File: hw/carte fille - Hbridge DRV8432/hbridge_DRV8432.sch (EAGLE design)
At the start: 37 parts, among them IC1 DRV8402

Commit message: Start routing the board
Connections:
- net GND: no longer C15.1, C16.1, C19.1, C20.1
- net GVDD: no longer R1.2, R11.2, R2.2, R3.2
- net N$1: no longer R3.1
- net N$16: now also IC1.RESET_AB; no longer IC1.RESET_CD, R11.1
- net N$17: now also IC1.PWM_B; no longer IC1.PWM_A
- net N$18: now also IC1.PWM_C; no longer IC1.PWM_B
- net N$19: now also IC1.RESET_CD; no longer IC1.PWM_C
- net N$6: no longer R2.1
- net N$8: now also IC1.PWM_A; no longer IC1.RESET_AB, R1.1
- net PVDD: no longer C15.2, C16.2, C19.2, C20.2
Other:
- moved on the sheet: SIGNAL

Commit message: rework board routing
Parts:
- removed C10, C11, C12, C13, C15, C16, C19, C20: 100nF - 0805, resistor:C-EUC0805
- removed C14: 100n, etienne:C_NP_805
- removed C18: 47uF, etienne:CPOL-EUE3.5-8
- removed C22: 330µF, etienne:CPOL-EUE3.5-8
- removed C5: 10nF - 0805, resistor:C-EUC0805
- removed SIGNAL: (no value), con-lsta:FE09-1
- added C17: 47u, rcl:CPOL-EUB/3528-21W
- added C21: 1u, rcl:C-EUC0805
- added C31, C32, C33, C34: 100n, rcl:C-EUC0805
- added C35, C36, C37, C38: 100n, rcl:C-EUC0603
- added H1, H2, H3, H4: MOUNT-HOLE3.2, holes:MOUNT-HOLE3.2
- added JP1: (no value), pinhead-2:PINHD-1X08_2.54
- added X4: M1-2, con-wago-500:W237-102
- added X5: M3-4, con-wago-500:W237-102
- added X6: +12V, con-wago-500:W237-102
- added X7: +24V, con-wago-500:W237-102
- C1: value 10nF - 0805 -> 10n; device resistor:C-EUC0805 -> rcl:C-EUC0805
- C2, C6, C8: value 1uF - 0805 -> 1u; device resistor:C-EUC0805 -> rcl:C-EUC0805
- C3: value 1000uF -> 1000u; device etienne:CPOL-EUE3.5-8 -> rcl:CPOL-EUE3.5-10
- C4: value 1000uF -> 100n; device etienne:CPOL-EUE3.5-8 -> rcl:C-EUC0603K
- C7: value 1uF -0805 -> 1u; device resistor:C-EUC0805 -> rcl:C-EUC0805
- C9: value 1uF - 0805 -> 330u; device resistor:C-EUC0805 -> rcl:CPOL-EUB/3528-21W
- R10: value 3R3 - 0603 -> 3.3; device resistor:R-EU_R0603 -> rcl:R-EU_R1206
- R12: value 3R3 - 0603 -> (none); device resistor:R-EU_R0603 -> rcl:R-EU_R0603
- R9: value 27K - 0603 -> 1; device resistor:R-EU_R0603 -> rcl:R-EU_R0603
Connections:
- removed net N$14: C5.1, R12.2
- removed net N$15: C13.1, IC1.BST_A
- removed net N$22: R5.1, X1-3.1
- removed net OUT_A: C13.2, IC1.OUT_A, X2-1.1
- removed net OUT_B: C12.2, IC1.OUT_B, X2-2.1
- removed net OUT_C: C11.2, IC1.OUT_C, X3-1.1
- removed net OUT_D: C10.2, IC1.OUT_D, X3-2.1
- new net GND1: X6-1.KL, X7-1.KL
- new net M1A: C33.1, IC1.OUT_A, X2-1.1, X4-1.KL
- new net M1B: C32.1, IC1.OUT_B, X2-2.1, X4-2.KL
- new net M1C: C31.2, IC1.OUT_C, X3-1.1, X5-1.KL
- new net M1D: C34.2, IC1.OUT_D, X3-2.1, X5-2.KL
- new net N$25: C33.2, IC1.BST_A
- new net N$26: C32.2, IC1.BST_B
- new net N$27: C31.1, IC1.BST_C
- new net N$28: C34.1, IC1.BST_D
- net GND: now also C1.1, C17.-, C2.1, C21.1, C35.1, C36.1, C37.1, C38.1, C6.1, C7.1, C8.1, C9.-, R9.1, X1-4.1; no longer C1.2, C14.1, C18.-, C2.2, C22.-, C4.-, C5.2, C6.2, C7.2, C8.2, C9.2, IC1.AGND, R4.2, R7.2, R8.2, R9.2, SIGNAL.1, X1-1.1
- net GVDD: now also C17.+, C2.2, C21.2, C6.2, C7.2, C8.2, C9.+; no longer C18.+, C2.1, C22.+, C6.1, C7.1, C8.1, C9.1
- net N$1: now also JP1.8; no longer SIGNAL.9
- net N$10: now also IC1.OC_ADJ, R12.2; no longer C12.1, IC1.BST_B
- net N$11: now also C4.1; no longer C14.2
- net N$12: now also X1-2.1; no longer C10.1, IC1.BST_D
- net N$13: now also C1.2, R10.1; no longer C1.1, R10.2
- net N$16: now also JP1.5; no longer SIGNAL.6
- net N$17: now also JP1.4; no longer SIGNAL.5
- net N$18: now also JP1.3; no longer SIGNAL.4
- net N$19: now also JP1.2; no longer SIGNAL.3
- net N$2: now also X1-1.1, X6-2.KL; no longer X1-2.1
- net N$20: now also JP1.1; no longer SIGNAL.2
- net N$6: now also JP1.7; no longer SIGNAL.8
- net N$7: now also R5.1, X1-3.1, X7-2.KL; no longer C11.1, IC1.BST_C
- net N$8: now also JP1.6; no longer SIGNAL.7
- net N$9: now also C4.2, IC1.AGND, R12.1, R4.2, R7.2, R8.2, R9.2; no longer IC1.OC_ADJ, R9.1
- net PVDD: now also C35.2, C36.2, C37.2, C38.2, R10.2; no longer C4.+, R10.1, R12.1
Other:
- moved on the sheet: C1, C2, C3, C6, C7, C8, R10, R12, R6, R9, X2-1, X2-2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

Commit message: wip
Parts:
- removed R5, R6: 0R, resistor:R-EU_R0603
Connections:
- removed net GND1: X6-1.KL, X7-1.KL
- removed net N$2: R6.1, X1-1.1, X6-2.KL
- removed net N$7: R5.1, X1-3.1, X7-2.KL
- net GND: now also X6-1.KL, X7-1.KL
- net GVDD: now also X1-1.1, X6-2.KL; no longer R6.2
- net PVDD: now also X1-3.1, X7-2.KL; no longer R5.2
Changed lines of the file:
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@@
 <part name="R7" library="resistor" deviceset="R-EU_" device="R0603" value="0R"/>
 <part name="R8" library="resistor" deviceset="R-EU_" device="R0603" value="0R"/>
-<part name="R6" library="resistor" deviceset="R-EU_" device="R0603" value="0R"/>
 <part name="GND8" library="supply1" deviceset="GND" device=""/>
 <part name="X1" library="con-phoenix-254" deviceset="MPT4" device=""/>
-<part name="R5" library="resistor" deviceset="R-EU_" device="R0603" value="0R"/>
 <part name="X2" library="con-phoenix-254" deviceset="MPT2" device=""/>
 <part name="X3" library="con-phoenix-254" deviceset="MPT2" device=""/>
@@
 <part name="X6" library="con-wago-500" deviceset="W237-102" device="" value="+12V"/>
 <part name="X7" library="con-wago-500" deviceset="W237-102" device="" value="+24V"/>
+<part name="GND2" library="supply1" deviceset="GND" device=""/>
 </parts>
 <sheets>
@@
 <instance part="R7" gate="G$1" x="-30.48" y="-12.7" rot="R180"/>
 <instance part="R8" gate="G$1" x="-30.48" y="-15.24" rot="R180"/>
-<instance part="R6" gate="G$1" x="-119.38" y="78.74"/>
 <instance part="GND8" gate="1" x="-124.46" y="73.66"/>
 <instance part="X1" gate="-1" x="-132.08" y="78.74" rot="R180"/>
@@
 <instance part="X1" gate="-3" x="-132.08" y="88.9" rot="R180"/>
 <instance part="X1" gate="-4" x="-132.08" y="93.98" rot="R180"/>
-<instance part="R5" gate="G$1" x="-121.92" y="88.9"/>
 <instance part="X2" gate="-1" x="58.42" y="7.62"/>
 <instance part="X2" gate="-2" x="58.42" y="2.54"/>
@@
 <instance part="X7" gate="-1" x="-119.38" y="45.72" rot="R180"/>
 <instance part="X7" gate="-2" x="-119.38" y="50.8" rot="R180"/>
+<instance part="GND2" gate="1" x="-134.62" y="27.94"/>
 </instances>
 <busses>
@@
 </segment>
 <segment>
-<pinref part="R5" gate="G$1" pin="2"/>
-<wire x1="-116.84" y1="88.9" x2="-109.22" y2="88.9" width="0.1524" layer="91"/>
 <label x="-114.3" y="88.9" size="1.778" layer="95"/>
+<pinref part="X7" gate="-2" pin="KL"/>
+<wire x1="-124.46" y1="50.8" x2="-127" y2="50.8" width="0.1524" layer="91"/>
+<wire x1="-127" y1="50.8" x2="-127" y2="88.9" width="0.1524" layer="91"/>
+<pinref part="X1" gate="-3" pin="1"/>
+<wire x1="-129.54" y1="88.9" x2="-127" y2="88.9" width="0.1524" layer="91"/>
+<wire x1="-127" y1="88.9" x2="-109.22" y2="88.9" width="0.1524" layer="91"/>
 </segment>
 <segment>
@@
 </segment>
 <segment>
+<pinref part="X1" gate="-4" pin="1"/>
+<wire x1="-124.46" y1="93.98" x2="-129.54" y2="93.98" width="0.1524" layer="91"/>
 <pinref part="GND8" gate="1" pin="GND"/>
-<pinref part="X1" gate="-4" pin="1"/>
 <wire x1="-124.46" y1="76.2" x2="-124.46" y2="93.98" width="0.1524" layer="91"/>
-<wire x1="-124.46" y1="93.98" x2="-129.54" y2="93.98" width="0.1524" layer="91"/>
+</segment>
+<segment>
+<wire x1="-124.46" y1="45.72" x2="-134.62" y2="45.72" width="0.1524" layer="91"/>
+<wire x1="-134.62" y1="45.72" x2="-134.62" y2="33.02" width="0.1524" layer="91"/>
+<wire x1="-124.46" y1="33.02" x2="-134.62" y2="33.02" width="0.1524" layer="91"/>
+<pinref part="X7" gate="-1" pin="KL"/>
+<pinref part="X6" gate="-1" pin="KL"/>
+<pinref part="GND2" gate="1" pin="GND"/>
+<wire x1="-134.62" y1="30.48" x2="-134.62" y2="33.02" width="0.1524" layer="91"/>
 </segment>
 </net>
@@
 </segment>
 <segment>
-<pinref part="R6" gate="G$1" pin="2"/>
-<wire x1="-114.3" y1="78.74" x2="-109.22" y2="78.74" width="0.1524" layer="91"/>
 <label x="-111.76" y="78.74" size="1.778" layer="95"/>
+<pinref part="X6" gate="-2" pin="KL"/>
+<wire x1="-124.46" y1="38.1" x2="-129.54" y2="38.1" width="0.1524" layer="91"/>
+<pinref part="X1" gate="-1" pin="1"/>
+<wire x1="-129.54" y1="38.1" x2="-129.54" y2="78.74" width="0.1524" layer="91"/>
+<wire x1="-129.54" y1="78.74" x2="-109.22" y2="78.74" width="0.1524" layer="91"/>
 </segment>
 <segment>
@@
 </segment>
 </net>
-<net name="N$2" class="0">
-<segment>
-<pinref part="X6" gate="-2" pin="KL"/>
-<wire x1="-124.46" y1="38.1" x2="-129.54" y2="38.1" width="0.1524" layer="91"/>
-<pinref part="X1" gate="-1" pin="1"/>
-<pinref part="R6" gate="G$1" pin="1"/>
-<wire x1="-129.54" y1="78.74" x2="-124.46" y2="78.74" width="0.1524" layer="91"/>
-<wire x1="-129.54" y1="38.1" x2="-129.54" y2="78.74" width="0.1524" layer="91"/>
-</segment>
-</net>
 <net name="N$1" class="0">
 <segment>
@@
 </segment>
 </net>
-<net name="GND1" class="0">
-<segment>
-<wire x1="-124.46" y1="45.72" x2="-134.62" y2="45.72" width="0.1524" layer="91"/>
-<wire x1="-134.62" y1="45.72" x2="-134.62" y2="33.02" width="0.1524" layer="91"/>
-<wire x1="-124.46" y1="33.02" x2="-134.62" y2="33.02" width="0.1524" layer="91"/>
-<pinref part="X7" gate="-1" pin="KL"/>
-<pinref part="X6" gate="-1" pin="KL"/>
-</segment>
-</net>
-<net name="N$7" class="0">
-<segment>
-<pinref part="R5" gate="G$1" pin="1"/>
-<pinref part="X7" gate="-2" pin="KL"/>
-<wire x1="-124.46" y1="50.8" x2="-127" y2="50.8" width="0.1524" layer="91"/>
-<wire x1="-127" y1="50.8" x2="-127" y2="88.9" width="0.1524" layer="91"/>
-<pinref part="X1" gate="-3" pin="1"/>
-<wire x1="-129.54" y1="88.9" x2="-127" y2="88.9" width="0.1524" layer="91"/>
-</segment>
-</net>

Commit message: finish routing
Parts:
- removed R1, R11, R2, R3: 10K - 0603, resistor:R-EU_R0603
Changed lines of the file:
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@@
 <part name="GND4" library="supply1" deviceset="GND" device=""/>
 <part name="GND6" library="supply1" deviceset="GND" device=""/>
-<part name="R11" library="resistor" deviceset="R-EU_" device="R0603" value="10K - 0603"/>
-<part name="R1" library="resistor" deviceset="R-EU_" device="R0603" value="10K - 0603"/>
-<part name="R2" library="resistor" deviceset="R-EU_" device="R0603" value="10K - 0603"/>
-<part name="R3" library="resistor" deviceset="R-EU_" device="R0603" value="10K - 0603"/>
 <part name="R4" library="resistor" deviceset="R-EU_" device="R0603" value="0R"/>
 <part name="R7" library="resistor" deviceset="R-EU_" device="R0603" value="0R"/>
@@
 <instance part="GND4" gate="1" x="-66.04" y="71.12"/>
 <instance part="GND6" gate="1" x="-15.24" y="60.96"/>
-<instance part="R11" gate="G$1" x="-43.18" y="27.94" rot="R90"/>
-<instance part="R1" gate="G$1" x="-38.1" y="27.94" rot="R90"/>
-<instance part="R2" gate="G$1" x="-33.02" y="27.94" rot="R90"/>
-<instance part="R3" gate="G$1" x="-27.94" y="27.94" rot="R90"/>
 <instance part="R4" gate="G$1" x="-30.48" y="-10.16" rot="R180"/>
 <instance part="R7" gate="G$1" x="-30.48" y="-12.7" rot="R180"/>

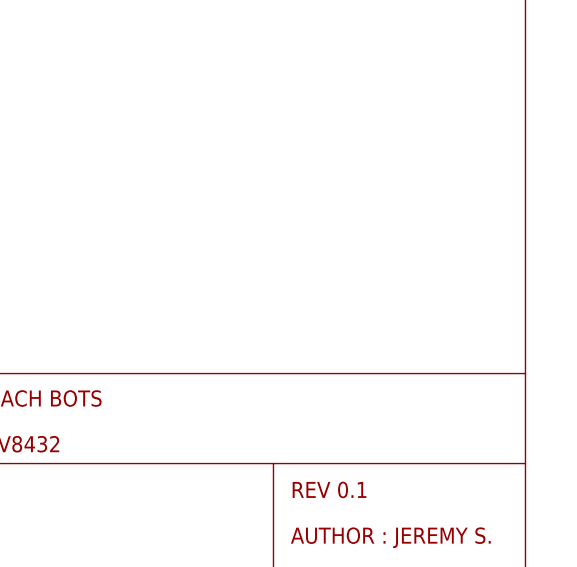
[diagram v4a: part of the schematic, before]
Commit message: add open hardware logo
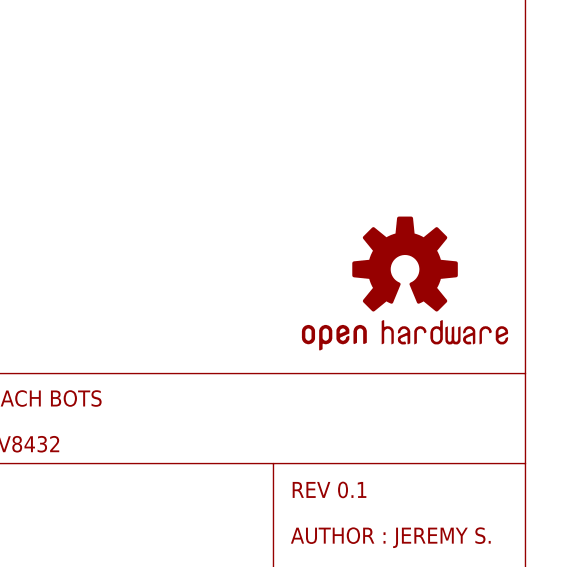
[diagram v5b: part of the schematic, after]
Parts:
- added U$1: OSHW-LOGOS, SparkFun-Aesthetics:OSHW-LOGOS
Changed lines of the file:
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@@
 <layer number="51" name="tDocu" color="7" fill="1" visible="no" active="no"/>
 <layer number="52" name="bDocu" color="7" fill="1" visible="no" active="no"/>
+<layer number="53" name="tGND_GNDA" color="7" fill="9" visible="no" active="no"/>
+<layer number="54" name="bGND_GNDA" color="1" fill="9" visible="no" active="no"/>
+<layer number="56" name="wert" color="7" fill="1" visible="no" active="no"/>
 <layer number="91" name="Nets" color="2" fill="1" visible="yes" active="yes"/>
 <layer number="92" name="Busses" color="1" fill="1" visible="yes" active="yes"/>
@@
 <layer number="99" name="SpiceOrder" color="5" fill="1" visible="yes" active="yes"/>
 <layer number="100" name="Muster" color="7" fill="1" visible="no" active="no"/>
+<layer number="101" name="Cutout" color="7" fill="1" visible="no" active="yes"/>
+<layer number="102" name="NoBridge" color="7" fill="1" visible="no" active="yes"/>
+<layer number="103" name="tMap" color="7" fill="1" visible="no" active="yes"/>
+<layer number="104" name="Name" color="16" fill="1" visible="no" active="yes"/>
+<layer number="105" name="tPlate" color="7" fill="1" visible="no" active="yes"/>
+<layer number="106" name="bPlate" color="7" fill="1" visible="no" active="yes"/>
+<layer number="107" name="Crop" color="7" fill="1" visible="no" active="yes"/>
+<layer number="116" name="Patch_BOT" color="9" fill="4" visible="no" active="yes"/>
+<layer number="120" name="DimPTH" color="7" fill="1" visible="no" active="yes"/>
+<layer number="121" name="_tsilk" color="7" fill="1" visible="no" active="yes"/>
+<layer number="122" name="_bsilk" color="7" fill="1" visible="no" active="yes"/>
+<layer number="125" name="_tNames" color="7" fill="1" visible="no" active="yes"/>
+<layer number="144" name="Drill_legend" color="7" fill="1" visible="no" active="yes"/>
+<layer number="151" name="HeatSink" color="7" fill="1" visible="no" active="yes"/>
+<layer number="200" name="200bmp" color="7" fill="1" visible="no" active="yes"/>
+<layer number="201" name="Tech2" color="7" fill="1" visible="no" active="yes"/>
+<layer number="202" name="Ref" color="7" fill="1" visible="no" active="yes"/>
+<layer number="203" name="203bmp" color="4" fill="10" visible="yes" active="yes"/>
+<layer number="204" name="204bmp" color="5" fill="10" visible="yes" active="yes"/>
+<layer number="205" name="205bmp" color="6" fill="10" visible="yes" active="yes"/>
+<layer number="206" name="206bmp" color="7" fill="10" visible="yes" active="yes"/>
+<layer number="207" name="207bmp" color="8" fill="10" visible="yes" active="yes"/>
+<layer number="208" name="208bmp" color="9" fill="10" visible="yes" active="yes"/>
+<layer number="209" name="209bmp" color="10" fill="10" visible="yes" active="yes"/>
+<layer number="210" name="210bmp" color="11" fill="10" visible="yes" active="yes"/>
+<layer number="211" name="211bmp" color="12" fill="10" visible="yes" active="yes"/>
+<layer number="212" name="212bmp" color="13" fill="10" visible="yes" active="yes"/>
+<layer number="213" name="213bmp" color="14" fill="10" visible="yes" active="yes"/>
+<layer number="214" name="214bmp" color="15" fill="10" visible="yes" active="yes"/>
+<layer number="215" name="215bmp" color="16" fill="10" visible="yes" active="yes"/>
+<layer number="216" name="216bmp" color="7" fill="1" visible="no" active="yes"/>
+<layer number="217" name="217bmp" color="18" fill="1" visible="no" active="no"/>
+<layer number="218" name="218bmp" color="19" fill="1" visible="no" active="no"/>
+<layer number="219" name="219bmp" color="20" fill="1" visible="no" active="no"/>
+<layer number="220" name="220bmp" color="21" fill="1" visible="no" active="no"/>
+<layer number="221" name="221bmp" color="22" fill="1" visible="no" active="no"/>
+<layer number="222" name="222bmp" color="23" fill="1" visible="no" active="no"/>
+<layer number="223" name="223bmp" color="24" fill="1" visible="no" active="no"/>
+<layer number="224" name="224bmp" color="25" fill="1" visible="no" active="no"/>
 <layer number="250" name="Descript" color="3" fill="1" visible="no" active="no"/>
 <layer number="251" name="SMDround" color="12" fill="11" visible="no" active="no"/>
+<layer number="254" name="cooling" color="7" fill="1" visible="no" active="yes"/>
 </layers>
 <schematic>
@@
 <part name="X7" library="con-wago-500" deviceset="W237-102" device="" value="+24V"/>
 <part name="GND2" library="supply1" deviceset="GND" device=""/>
+<part name="U$1" library="SparkFun-Aesthetics" deviceset="OSHW-LOGO" device="S"/>
 </parts>
 <sheets>
@@
 <instance part="X7" gate="-2" x="-119.38" y="50.8" rot="R180"/>
 <instance part="GND2" gate="1" x="-134.62" y="27.94"/>
+<instance part="U$1" gate="G$1" x="134.62" y="-58.42"/>
 </instances>
 <busses>
